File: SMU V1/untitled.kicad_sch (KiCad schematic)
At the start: 3 parts, among them U1101 AMS1117-3.3

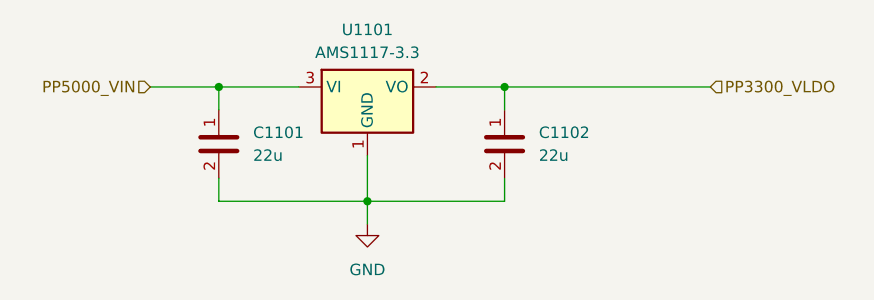
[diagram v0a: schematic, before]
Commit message: halfway done with routing, still needs antenna
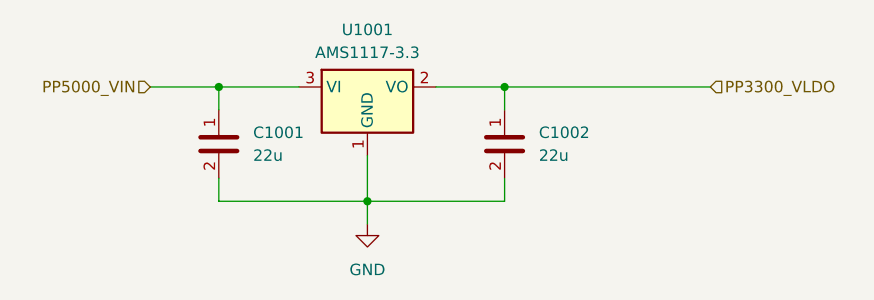
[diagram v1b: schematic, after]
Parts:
- renumbered C1101 to C1001, C1102 to C1002, U1101 to U1001
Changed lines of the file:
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@@
 		(dnp no)
 		(fields_autoplaced yes)
-		(property "Reference" "C1101"
+		(property "Reference" "C1001"
 			(at 113.03 81.2799 0)
 			(effects
@@
 			(project "SMU V1"
 				(path "/1f58b889-96e6-4877-90a3-5a655db5910b/b9f10619-4e5b-45af-b866-c6815d605ed5/e5fde666-5538-4e83-833b-79c3c9c21c9e"
-					(reference "C1101")
+					(reference "C1001")
 					(unit 1)
 				)
@@
 		(dnp no)
 		(fields_autoplaced yes)
-		(property "Reference" "U1101"
+		(property "Reference" "U1001"
 			(at 125.73 69.85 0)
 			(effects
@@
 			(project "SMU V1"
 				(path "/1f58b889-96e6-4877-90a3-5a655db5910b/b9f10619-4e5b-45af-b866-c6815d605ed5/e5fde666-5538-4e83-833b-79c3c9c21c9e"
-					(reference "U1101")
+					(reference "U1001")
 					(unit 1)
 				)
@@
 		(dnp no)
 		(fields_autoplaced yes)
-		(property "Reference" "#PWR01101"
+		(property "Reference" "#PWR01001"
 			(at 125.73 97.79 0)
 			(effects
@@
 			(project "SMU V1"
 				(path "/1f58b889-96e6-4877-90a3-5a655db5910b/b9f10619-4e5b-45af-b866-c6815d605ed5/e5fde666-5538-4e83-833b-79c3c9c21c9e"
-					(reference "#PWR01101")
+					(reference "#PWR01001")
 					(unit 1)
 				)
@@
 		(dnp no)
 		(fields_autoplaced yes)
-		(property "Reference" "C1102"
+		(property "Reference" "C1002"
 			(at 144.78 81.2799 0)
 			(effects
@@
 			(project "SMU V1"
 				(path "/1f58b889-96e6-4877-90a3-5a655db5910b/b9f10619-4e5b-45af-b866-c6815d605ed5/e5fde666-5538-4e83-833b-79c3c9c21c9e"
-					(reference "C1102")
+					(reference "C1002")
 					(unit 1)
 				)
